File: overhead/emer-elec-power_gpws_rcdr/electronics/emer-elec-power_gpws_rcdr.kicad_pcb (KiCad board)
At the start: 2 copper layers, 145 x 133.9 mm, 94 parts, among them J1 Conn_02x01, J2 Conn_02x13_Counter_Clockwise, J3 Conn_02x01, J4 Conn_02x01, J5 Conn_02x01, J6 Conn_02x01

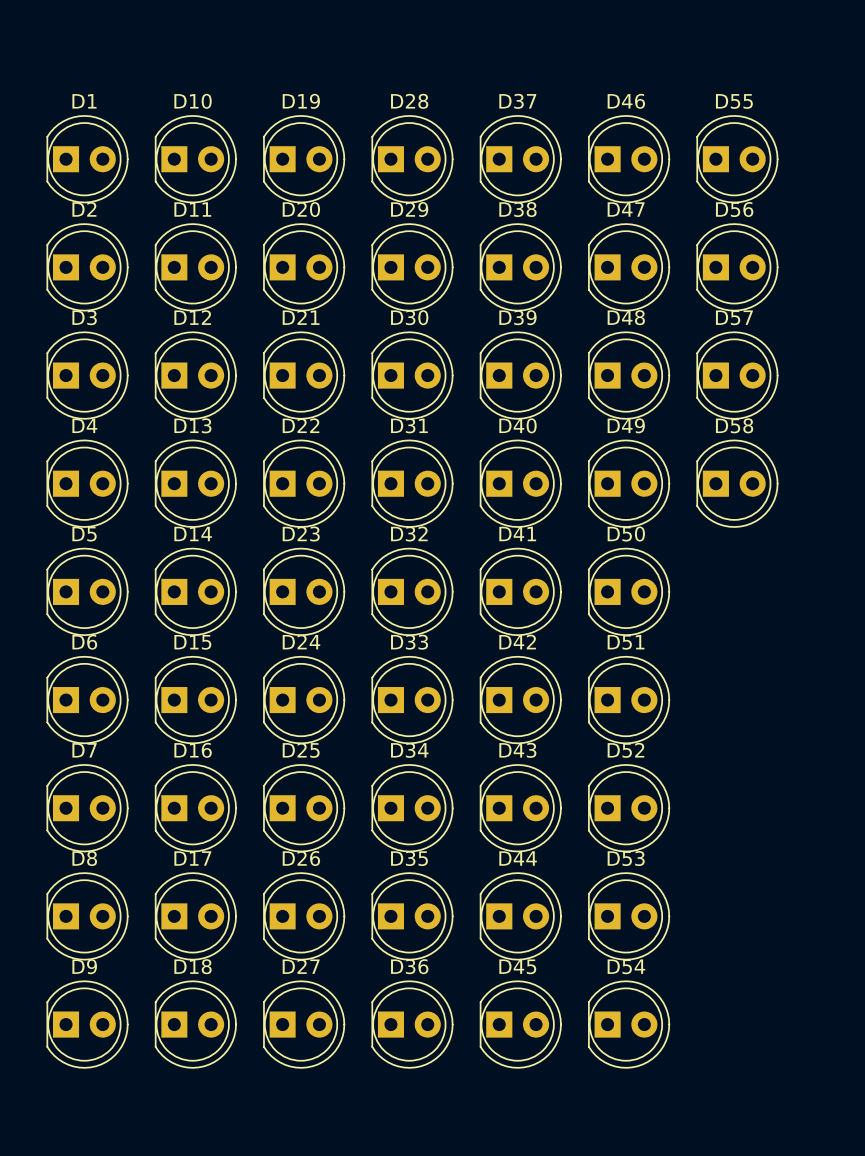
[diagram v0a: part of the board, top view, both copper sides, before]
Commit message: Updated all LEDs for SMD!
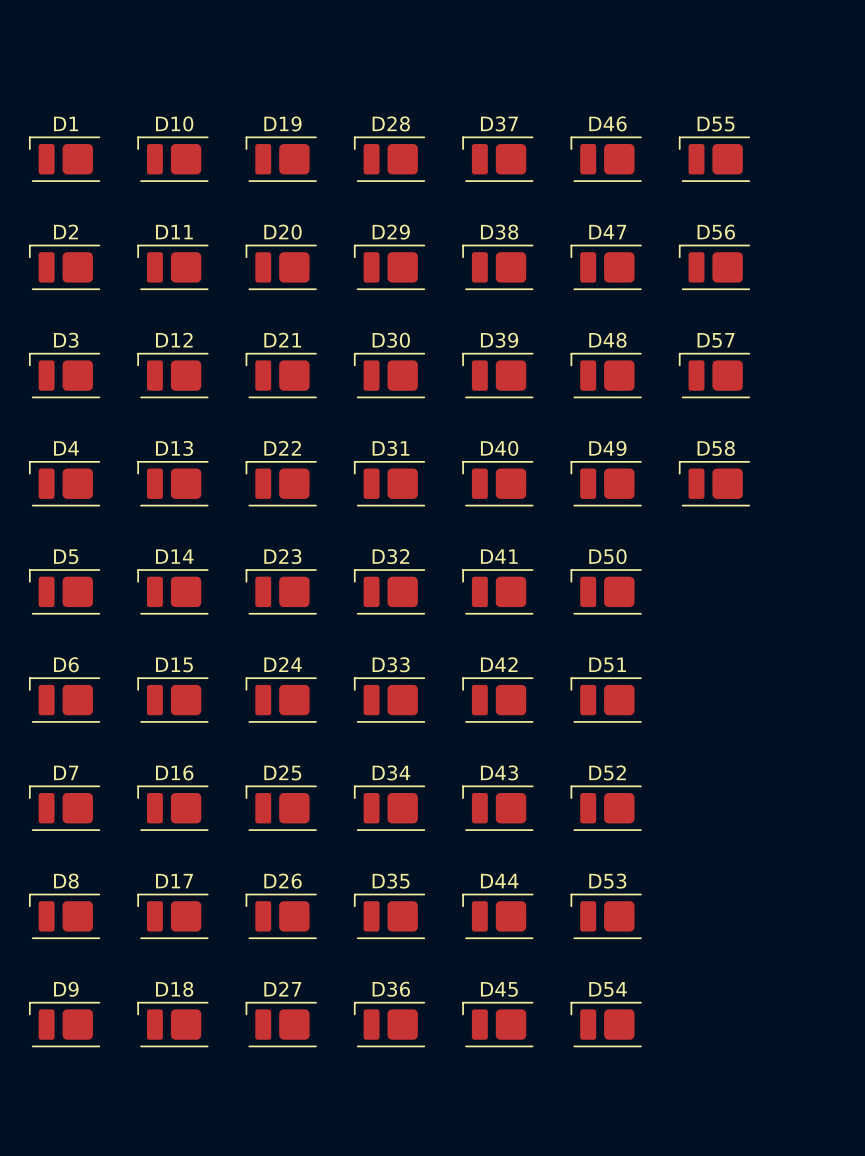
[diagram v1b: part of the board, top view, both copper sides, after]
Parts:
- D1, D10, D11, D12, D13, D14, D15, D16, D17, D18, D19, D2, D20, D21, D22, D23, D24, D25, D26, D27, D28, D29, D3, D30, D31, D32, D33, D34, D35, D36, D37, D38, D39, D4, D40, D41, D42, D43, D44, D45, D46, D47, D48, D49, D5, D50, D51, D52, D53, D54, D55, D56, D57, D58, D6, D7, D8, D9: footprint LED_THT:LED_D5.0mm_Clear -> OpenA3XX:LED_Everlight-SMD3528_3.5x2.8mm_67-21ST

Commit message: EMER ELEC POWER GPWS RCDR Panel
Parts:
- removed D53, D54, D55, D56, D57, D58: LED, OpenA3XX:LED_Everlight-SMD3528_3.5x2.8mm_67-21ST
- removed R19, R20: 220R, Resistor_SMD:R_1206_3216Metric_Pad1.30x1.75mm_HandSolder
- J1: moved to B.Cu
- moved D16 221.5 mm to (195.4, 45.9)
- moved D17 216.0 mm to (195.2, 72.9)
- moved D21 213.8 mm to (204.9, 60.3)
- moved D47 209.1 mm to (209.5, 155.3)
- moved D20 208.2 mm to (200.8, 81.1)
- moved D40 207.7 mm to (214.9, 106.6)
- moved D46 206.4 mm to (210.6, 137.0)
- moved D30 201.7 mm to (201.5, 97.4)
- moved D38 201.0 mm to (203.7, 122.6)
- moved D52 200.8 mm to (211.4, 73.6)
- moved D14 199.3 mm to (179.1, 54.7)
- moved D25 197.3 mm to (188.2, 89.2)
- moved D15 196.7 mm to (178.8, 73.8)
- moved D11 193.4 mm to (174.9, 40.8)
- moved D18 189.6 mm to (168.1, 80.9)
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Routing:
- net GND: track 0.00 -> 758.1 mm, vias 0 -> 6
- net +12V: track 0.00 -> 579.0 mm, vias 0 -> 14
- net Net-(J2-Pin_6): track 0.00 -> 202.0 mm, vias 0 -> 2
- net Net-(J2-Pin_4): track 0.00 -> 180.4 mm, vias 0 -> 1
- net Net-(J2-Pin_24): track 0.00 -> 169.4 mm, vias 0 -> 1
- net Net-(J2-Pin_5): track 0.00 -> 167.8 mm, vias 0 -> 1
- net Net-(D51-K): track 0.00 -> 162.5 mm, vias 0 -> 2
- net Net-(J2-Pin_22): track 0.00 -> 150.1 mm, vias 0 -> 1
- net Net-(J2-Pin_14): track 0.00 -> 148.9 mm, vias 0 -> 3
- net Net-(J2-Pin_15): track 0.00 -> 147.4 mm, vias 0 -> 1
- net Net-(J2-Pin_23): track 0.00 -> 142.4 mm, vias 0 -> 1
- net Net-(J2-Pin_13): track 0.00 -> 135.0 mm, vias 0 -> 1
- net Net-(J2-Pin_8): track 0.00 -> 128.5 mm, vias 0 -> 2
- net Net-(D19-K): track 0.00 -> 127.7 mm
- net Net-(J2-Pin_9): track 0.00 -> 127.1 mm, vias 0 -> 1
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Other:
- outline, holes or cut-outs redrawn
- board text added: "+12V Variable Backlight"
- board text added: "1"
- board text added: "2"
- board text added: "27"
- board text added: "28"
- board text added: "GND"

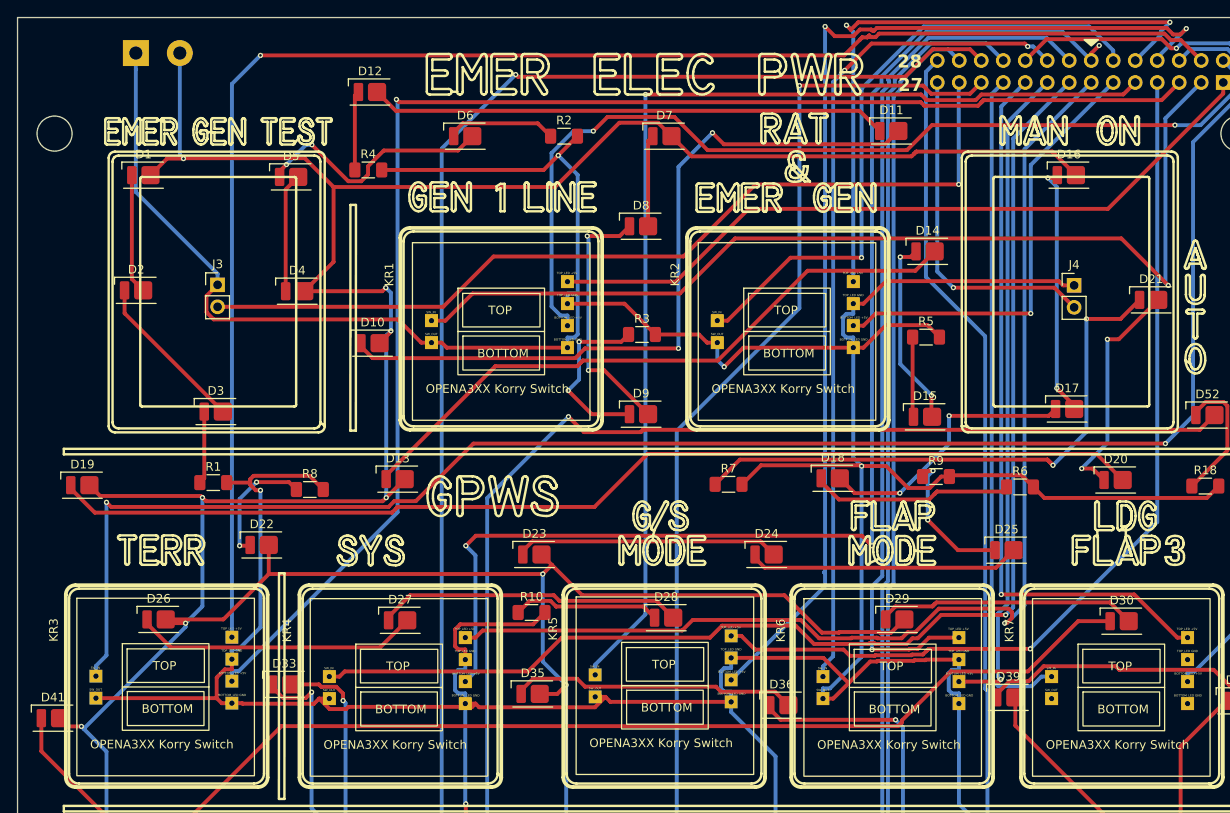
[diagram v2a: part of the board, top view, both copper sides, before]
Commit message: Fixed minor mistake + Created preliminary work for OXYGEN CALLS RAIN RPLNT WIPERS Panel
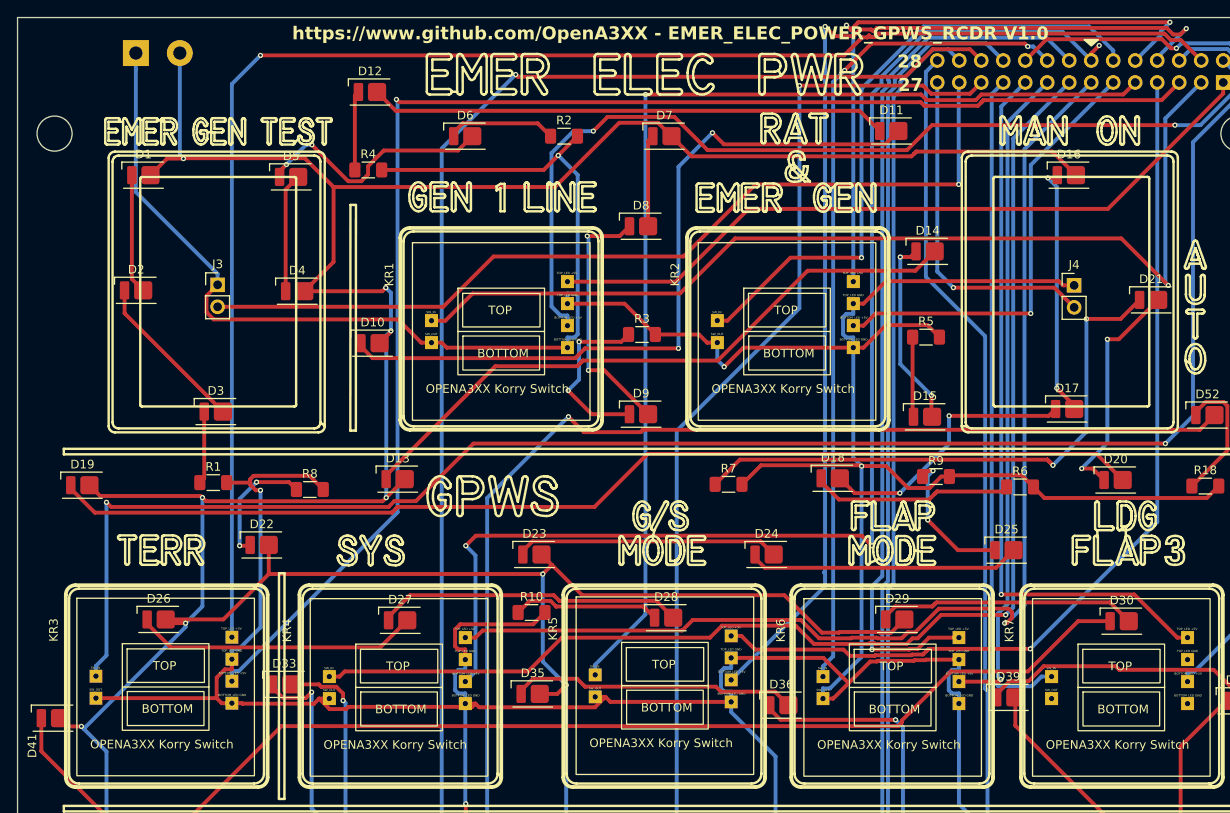
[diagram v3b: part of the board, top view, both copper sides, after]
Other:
- board text added: "https://www.github.com/OpenA3XX - EMER_ELEC_POWER_GPWS_RCDR V1.0"
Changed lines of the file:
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@@
 		(tags "LED 3528")
 		(property "Reference" "D41"
-			(at 0 -2.4 0)
+			(at -2.39 3.2 90)
 			(layer "F.SilkS")
 			(effects
@@
 		)
 	)
+	(gr_text "https://www.github.com/OpenA3XX - EMER_ELEC_POWER_GPWS_RCDR V1.0"
+		(at 105.7 30.4 0)
+		(layer "F.SilkS")
+		(effects
+			(font
+				(size 1.5 1.5)
+				(thickness 0.3)
+				(bold yes)
+			)
+			(justify left bottom)
+		)
+	)
 	(gr_text "Flight Simulation Only"
 		(at 75.3 142.9 0)
@@
 		)
 	)
+	(gr_text "https://www.github.com/OpenA3XX - EMER_ELEC_POWER_GPWS_RCDR V1.0"
+		(at 189 160.6 0)
+		(layer "B.SilkS")
+		(effects
+			(font
+				(size 1.5 1.5)
+				(thickness 0.3)
+				(bold yes)
+			)
+			(justify left bottom mirror)
+		)
+	)
